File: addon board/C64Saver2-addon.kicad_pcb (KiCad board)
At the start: 2 copper layers, 43.9 x 29 mm, 41 parts, among them CON1 AVR-ISP-6, J1 Conn_01x08_Female, J2 Conn_01x08_Female, J3 OLED_128x32_Conn_01x04_Male, J4 Conn_01x04_Female, SW1 SW_Push, U1 INA219xIDR-SOIC, U2 ISO1541D, U3 ATTINY85-20SU, U4 TLP291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

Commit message: addonboard: 5V moved to VIN+, and fixed SDA2 and SCL2. #16 #17
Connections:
- C6 pad 2: VIN- -> /VIN+
- R7 pad 1: /SDA2 -> Net-(R7-Pad1)
- R9 pad 1: /SCL2 -> Net-(R9-Pad1)
- U1 pad 3: /SCL2 -> /SDA2
- U1 pad 4: /SDA2 -> /SCL2
- U8 pad 3: VIN- -> /VIN+
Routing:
- net VIN-: track 62.3 -> 34.5 mm
- net /VIN+: track 18.2 -> 31.8 mm
- net /SCL2: track 24.2 -> 14.6 mm
- net Net-(R7-Pad1): track 0.00 -> 1.93 mm
- net /SDA2: track 14.9 -> 13.8 mm
- net Net-(R9-Pad1): track 0.00 -> 1.00 mm
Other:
- board text added: "1.2"
- board text added: "2018-11-04"
- board text removed: "1.1"
- board text removed: "2018-09-23"

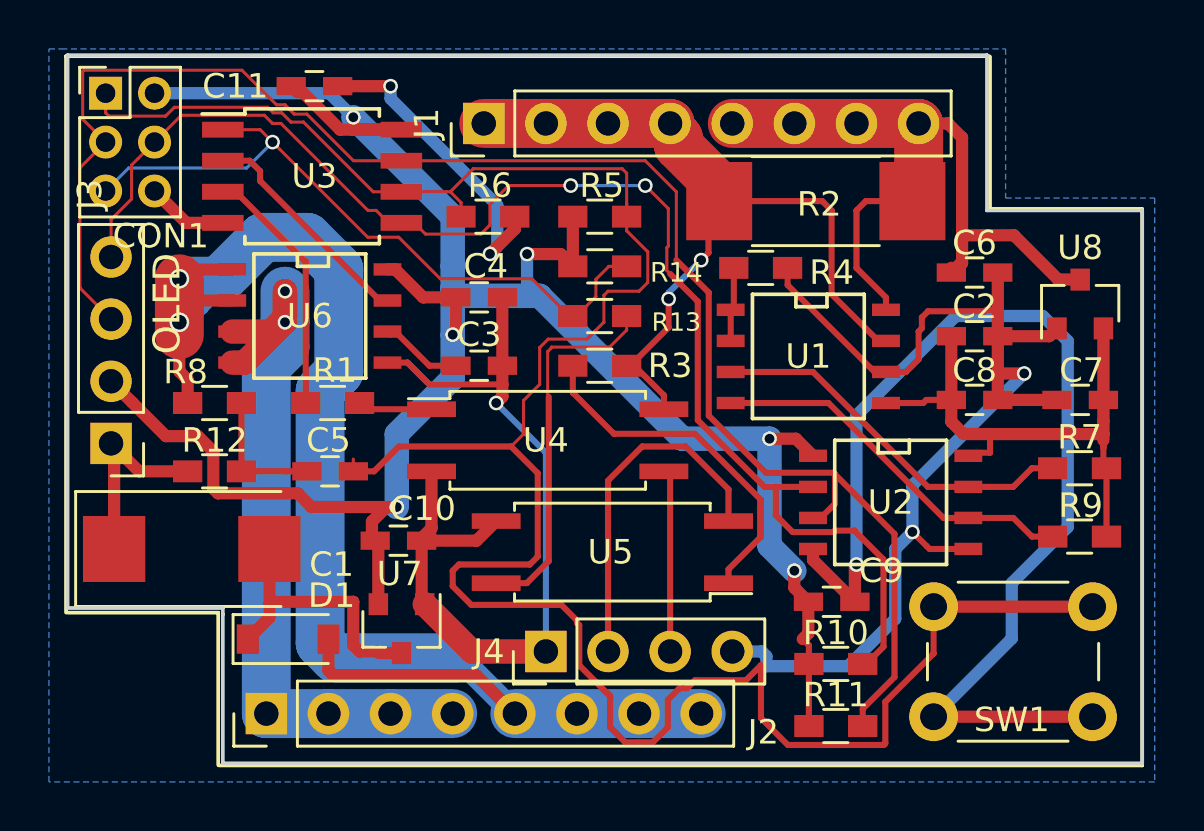
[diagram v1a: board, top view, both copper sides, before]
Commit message: Swapped HOLD_ with SENSE_VAC #18
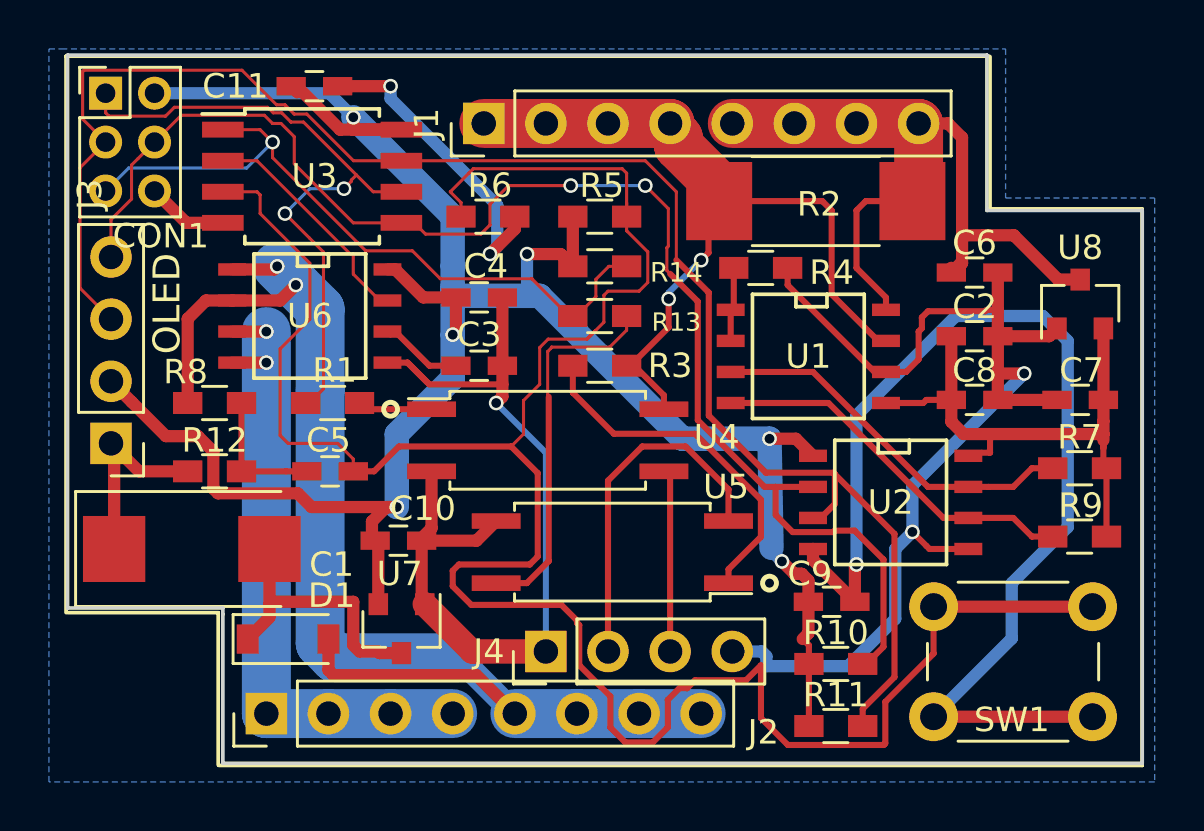
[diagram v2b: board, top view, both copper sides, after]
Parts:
- R10, R11, R7, R9: value 560 -> 4k7
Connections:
- CON1 pad 1: /SENSE_VAC -> /HOLD_
- R7 pad 1: Net-(R7-Pad1) -> /SDA2
- R9 pad 1: Net-(R9-Pad1) -> /SCL2
- U3 pad 3: /HOLD_ -> /SENSE_VAC
- U3 pad 6: /SENSE_VAC -> /HOLD_
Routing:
- net /HOLD_: track 10.3 -> 27.5 mm, vias 0 -> 2
- net /9VAC1+: track 67.2 -> 53.2 mm
- net /9VAC1-: track 32.8 -> 27.3 mm
- net Net-(R7-Pad1): track 1.93 -> 0.00 mm
- net /SDA2: track 13.8 -> 15.7 mm
- net Net-(R9-Pad1): track 1.00 -> 0.00 mm
- net /SCL2: track 14.6 -> 15.6 mm
- net /SDA1: track 57.1 -> 57.7 mm
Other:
- board text added: "2018-11-11"
- board text added: "C64 Saver 2 - Addon Board Rev 1.2 BWACK 2018"
- board text removed: "2018-11-04"
- board text removed: "C64 Saver Addon Rev 1.1 BWACK 2018"

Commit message: MLCC 1210 cap and optoisolators changed to Package_SO:SOIC-4_4.55x2.6mm_P1.27mm
Not finished routing. Needs more of the 1210 caps.
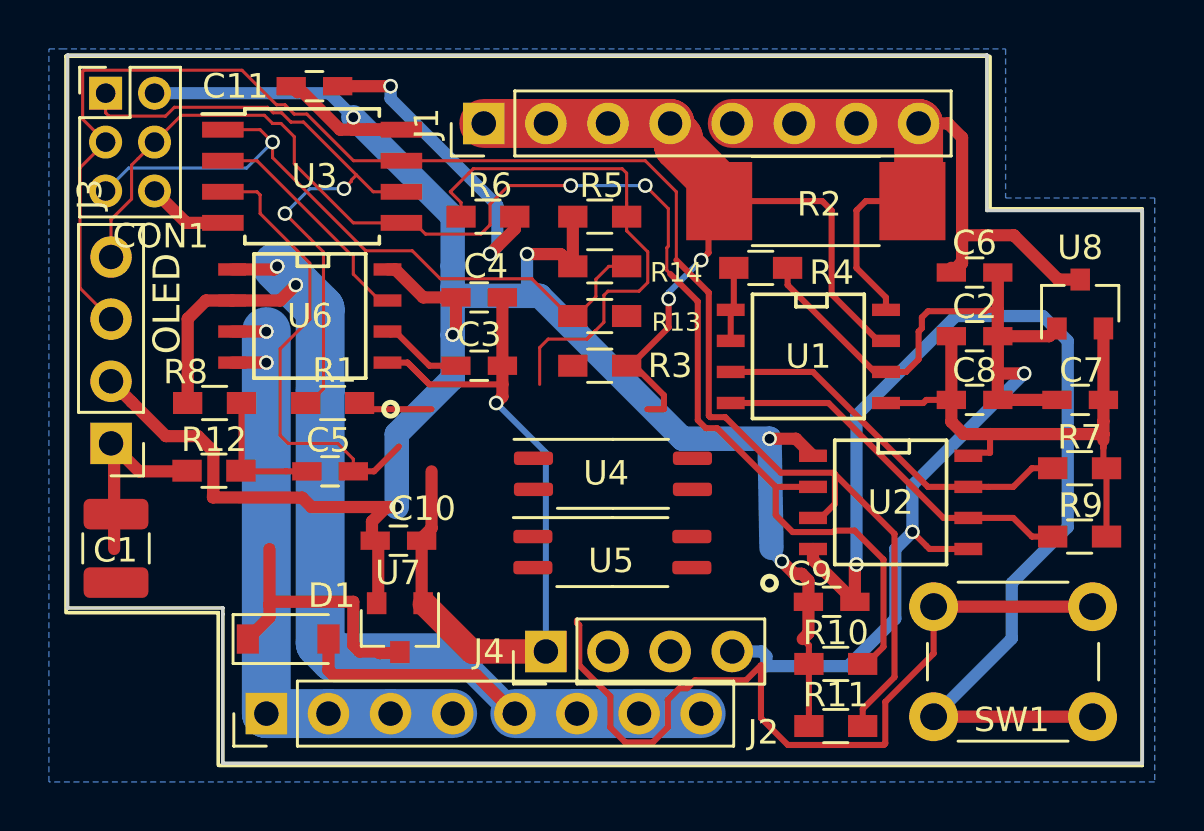
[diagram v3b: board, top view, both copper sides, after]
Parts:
- C1: footprint Capacitors_Tantalum_SMD:CP_Tantalum_Case-X_EIA-7343-43_Reflow -> Capacitor_SMD:C_1210_3225Metric
- U4, U5: footprint Housings_SOIC:SO-4_7.6x3.6mm_Pitch2.54mm -> Package_SO:SOIC-4_4.55x2.6mm_P1.27mm
- moved C1 3.10 mm to (142.4, 103.7), turned to 90 degrees
- moved U4 3.00 mm to (162.8, 100.7)
- moved U7 0.08 mm to (154.1, 107.0)
- turned U5 to 0 degrees
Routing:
- net /SENSE_VAC: track 98.8 -> 76.2 mm
- net Net-(R13-Pad2): track 16.0 -> 0.00 mm
- net Net-(R3-Pad1): track 15.2 -> 0.00 mm
- net OVERVOLTAGE: track 14.5 -> 0.00 mm
- net PGATE: track 7.47 -> 0.00 mm
- net GND: track 108.0 -> 104.4 mm
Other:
- rule pad_to_mask_clearance: 0.2 -> 0.1
- board text removed: "1.2"
- board text removed: "2018-11-11"
- board text removed: "C64 Saver addon board"

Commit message: Addon Board 1.3 (2019-05-24)
  - Changed optocoupler footprint to more common SOIC-4_4.55x2.6mm_P1.27mm
  - Larger 5V regulator on 9vac side for less heat
  - replaced 100uF tantalum with 3x 47uF 1206 MLCC
  - kicad 5.1.0 project
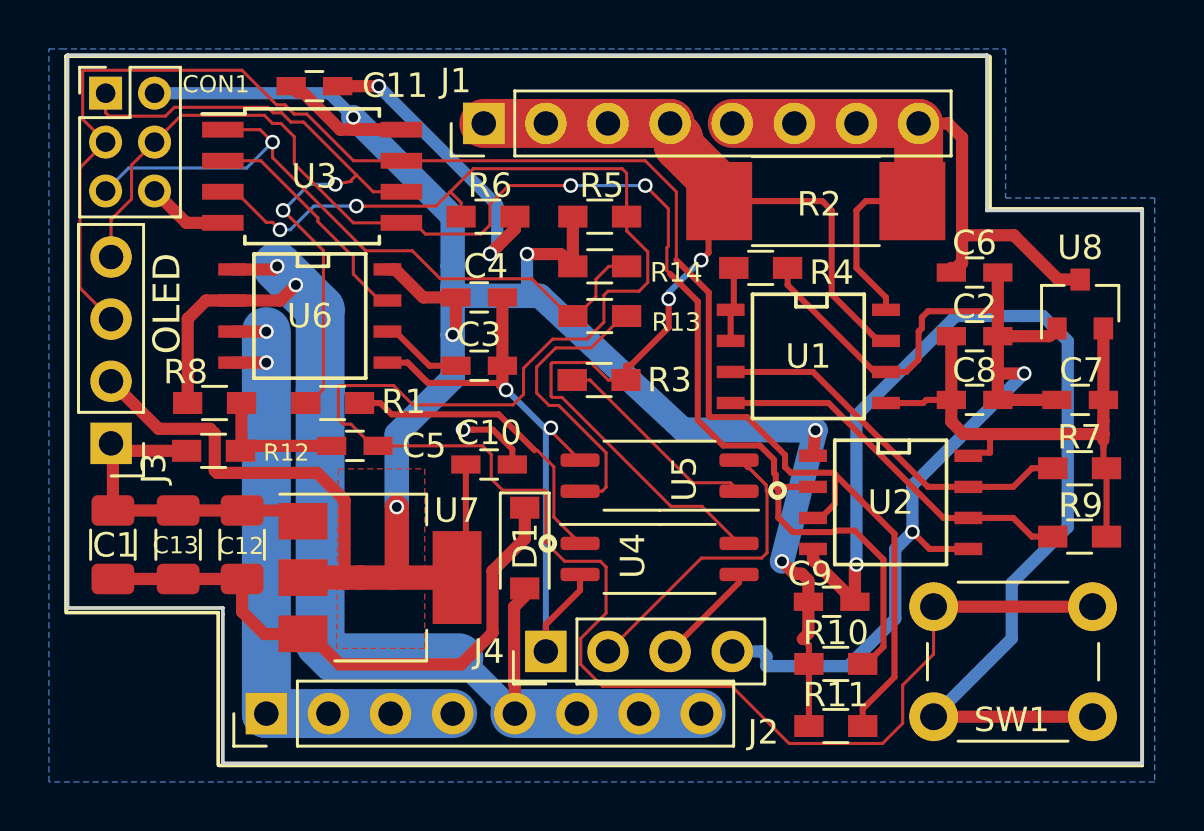
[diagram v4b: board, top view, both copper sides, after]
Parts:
- added C12: 47uF, Capacitor_SMD:C_1206_3216Metric, F.Cu at (147.6, 103.6)
- added C13: 47uF, Capacitor_SMD:C_1206_3216Metric, F.Cu at (145.0, 103.6)
- C1: value 220u -> 47uF; footprint Capacitor_SMD:C_1210_3225Metric -> Capacitor_SMD:C_1206_3216Metric
- D1: value D -> Dotec SL1G
- U4, U5: value TLP291 -> ACPL-217-50DE
- U7: footprint TO_SOT_Packages_SMD:SOT-23 -> Package_TO_SOT_SMD:SOT-223-3_TabPin2
- moved D1 10.4 mm to (159.2, 103.7), turned to 270 degrees
- moved C10 4.84 mm to (157.7, 100.3)
- moved U4 3.97 mm to (164.7, 104.2)
- moved U5 3.67 mm to (164.7, 100.8), turned to 180 degrees
- moved U7 2.20 mm to (153.2, 104.9), turned to 0 degrees
- moved C5 1.45 mm to (152.2, 99.5)
- moved R12 0.81 mm to (146.4, 99.7)
- moved R3 0.58 mm to (162.2, 96.9)
- moved C1 0.20 mm to (142.3, 103.6)
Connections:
- C1 pad 1: GND -> Net-(C1-Pad1)
- C1 pad 2: Net-(C1-Pad2) -> GND
- D1 pad 1: Net-(C1-Pad2) -> Net-(C1-Pad1)
- U7 pad 3: Net-(C1-Pad2) -> Net-(C1-Pad1)
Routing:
- net Net-(C1-Pad1): track 0.00 -> 23.6 mm
- net OVERVOLTAGE: track 0.00 -> 13.4 mm
- net /SENSE_VAC: track 76.2 -> 89.5 mm, vias 0 -> 2
- net VIN-: track 34.5 -> 46.7 mm
- net Net-(R13-Pad2): track 0.00 -> 12.0 mm
- net Net-(C1-Pad2): track 11.4 -> 0.00 mm
- net +5V: track 96.7 -> 107.6 mm
- net /HOLD: track 3.05 -> 13.0 mm
- net Net-(R3-Pad1): track 0.00 -> 8.70 mm
- net /9VAC1+: track 53.2 -> 48.6 mm
- net PGATE: track 0.00 -> 4.32 mm
- net GND: track 104.4 -> 106.8 mm, vias 4 -> 6
- net /SDA1: track 57.7 -> 58.4 mm
- added copper zone on F.Cu, net +5V

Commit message: year and version on silkscreen
switched to kicad 5.1.0 -> 5.1.2
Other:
- board text added: "C64 Saver 2 - Addon Board Rev 1.3 BWACK 2018-2019"
- board text removed: "C64 Saver 2 - Addon Board Rev 1.2 BWACK 2018"
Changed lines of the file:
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@@
-(kicad_pcb (version 20171130) (host pcbnew "(5.1.0)-1")
+(kicad_pcb (version 20171130) (host pcbnew "(5.1.2)-1")
   (general
     (thickness 1.6)
@@
     (effects (font (size 1.1 1.1) (thickness 0.275)))
   )
-  (gr_text "C64 Saver 2 -\nAddon Board\nRev 1.2 BWACK 2018" (at 178.689 93.726) (layer B.SilkS)
+  (gr_text "C64 Saver 2 -\nAddon Board\nRev 1.3 BWACK 2018-2019" (at 178.689 93.726) (layer B.SilkS)
     (effects (font (size 1.25 1.25) (thickness 0.3)) (justify left mirror))
   )

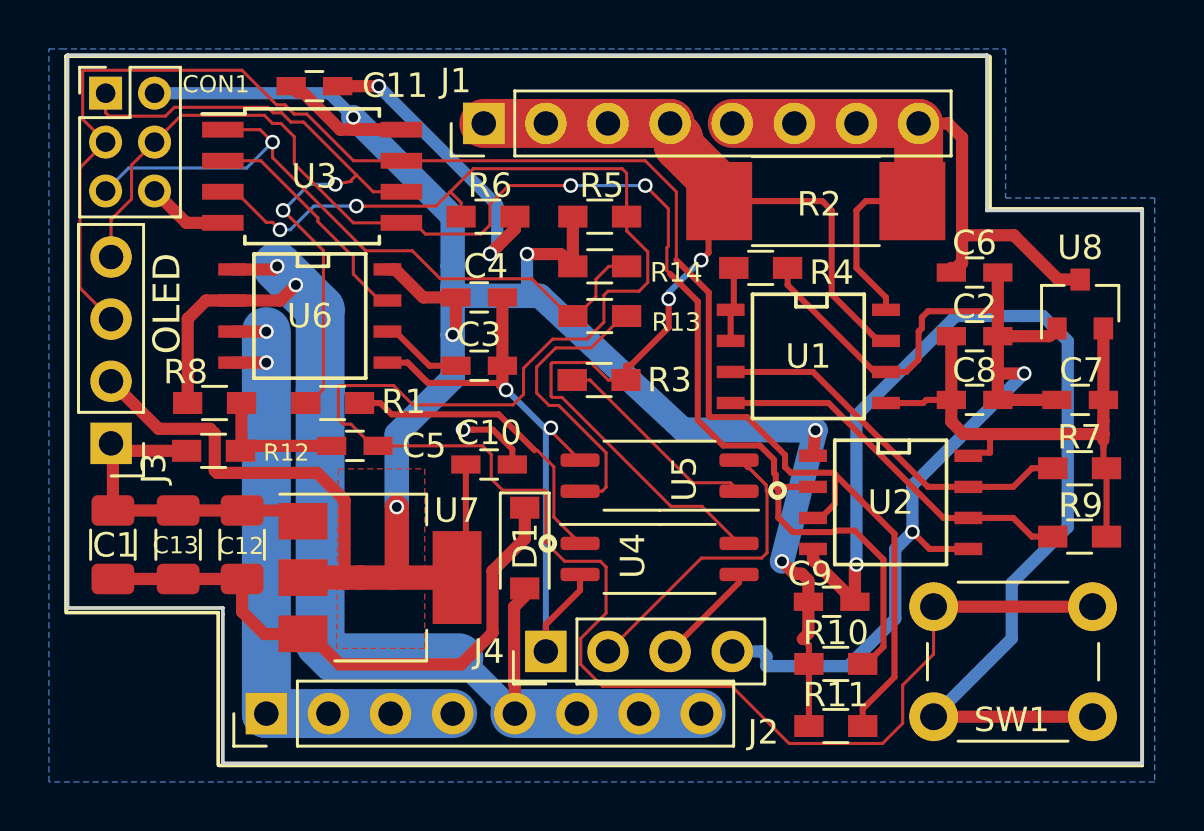
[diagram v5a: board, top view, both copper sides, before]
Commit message: kicad 5.1.0 -> 5.1.2
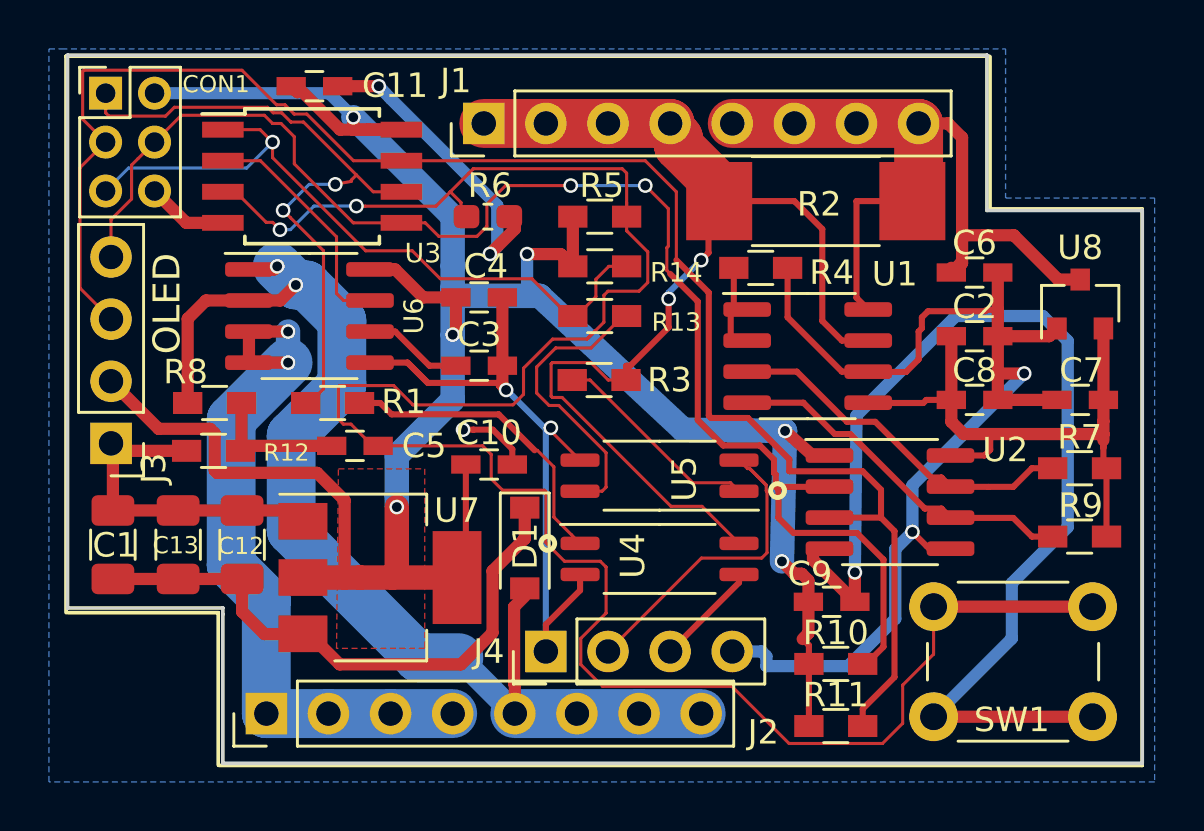
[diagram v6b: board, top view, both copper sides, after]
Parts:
- R6: footprint Resistors_SMD:R_0603_HandSoldering -> Resistor_SMD:R_0603_1608Metric_Pad1.05x0.95mm_HandSolder
- U1, U2, U6: footprint SMD_Packages:SOIC-8-N -> Package_SO:SOIC-8_3.9x4.9mm_P1.27mm
- U3: footprint Housings_SOIC:SOIJ-8_5.3x5.3mm_Pitch1.27mm -> Package_SO:SOIJ-8_5.3x5.3mm_P1.27mm
- turned U1 to 0 degrees
- turned U2 to 0 degrees
- turned U6 to 0 degrees
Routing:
- net /9VAC1-: track 27.3 -> 32.1 mm
- net +5V: track 107.6 -> 109.6 mm
- net /SDA2: track 15.7 -> 14.0 mm
- net /VDD2: track 22.8 -> 24.1 mm
- net GNDD: track 47.2 -> 47.7 mm
- net /SCL1: track 68.1 -> 68.7 mm
